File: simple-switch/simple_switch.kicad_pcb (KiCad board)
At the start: 4 copper layers, 25.4 x 40.6 mm, 20 parts, among them J1 CON_HDR_100MILS_M_TH_2X8, J2 CON_TERM_BLK_1X2_TB008A-508-0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, Q1 TRX_NMOS_PJD40N04_L2_00001, Q2 TRX_NMOS_PJD40N04_L2_00001, Q3 TRX_NMOS_PJD40N04_L2_00001, Q4 TRX_NMOS_PJD40N04_L2_00001, U1 DRV_A4957SESTR-T

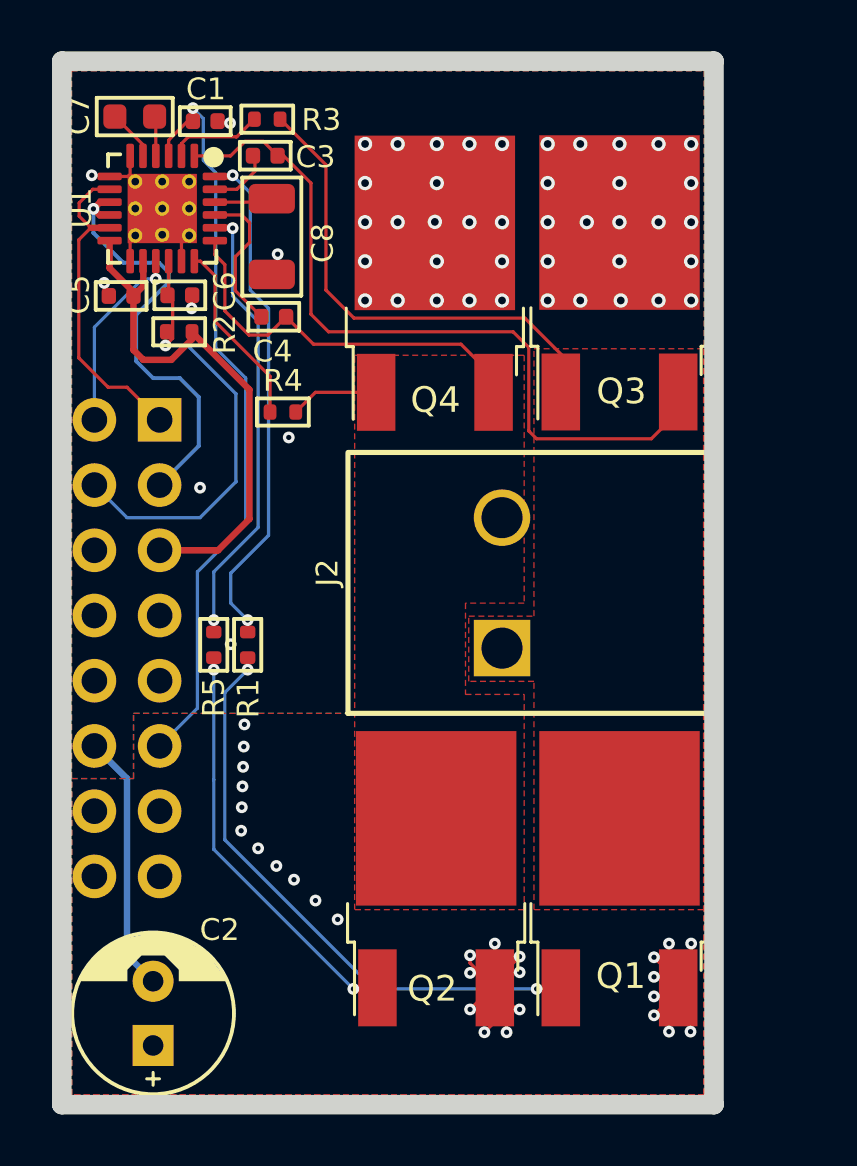
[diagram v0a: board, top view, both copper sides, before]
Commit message: rename project, comple simple switch layout, fix thermal reliefs
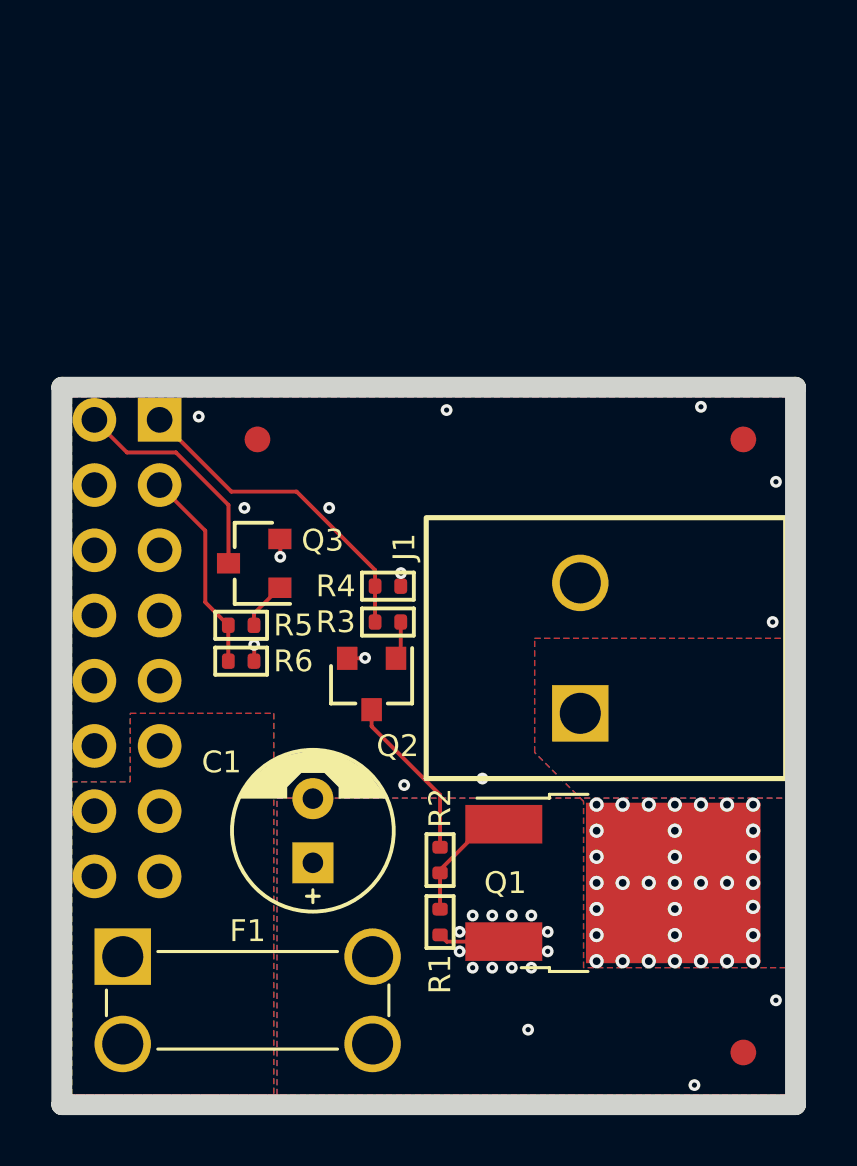
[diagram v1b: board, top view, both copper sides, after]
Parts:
- removed C2: CAP_AE_22UF_100V_TH_6.3MM, connaxio-capacitors:CAP_AE_RAD_D6.3_H12.5_P2.5
- removed C3, C4, C5, C6: CAP_CER_100NF_25V_0402, connaxio-capacitors:CAP_CER_0402_1005M
- removed C7: CAP_CER_1UF_25V_0603, connaxio-capacitors:CAP_CER_0603_1608M
- removed C8: CAP_CER_10UF_25V_1206, connaxio-capacitors:CAP_CER_1206_3216M
- removed Q4: TRX_NMOS_PJD40N04_L2_00001, connaxio-sop:TO-252-3
- removed U1: DRV_A4957SESTR-T, connaxio-fp:QFN-24_4x4_P0.5_EP2.7X2.7
- added F1: FUS_BLADE_MINI_3588-1, connaxio-connectors:FUS_BLADE_MINI_3588-1, F.Cu at (121.2, 84.8)
- added F2: FID_1X3, connaxio-mechanical:FID_1X3, F.Cu at (121.5, 63.0)
- added F3: FID_1X3, connaxio-mechanical:FID_1X3, F.Cu at (140.5, 63.0)
- added F4: FID_1X3, connaxio-mechanical:FID_1X3, F.Cu at (140.5, 86.9)
- added R6: RES_12.4KΩ_1%_0402, connaxio-resistors:RES_0402_1005M, F.Cu at (120.9, 71.6)
- C1: value CAP_CER_100NF_25V_0402 -> CAP_AE_22UF_100V_TH_6.3MM; footprint connaxio-capacitors:CAP_CER_0402_1005M -> connaxio-capacitors:CAP_AE_RAD_D6.3_H12.5_P2.5
- J1: value CON_HDR_100MILS_M_TH_2X8 -> CON_TERM_BLK_1X2_TB008A-508-02BE; footprint connaxio-connectors:CON_HDR_100MILS_M_TH_2X8 -> connaxio-connectors:CON_TERM_BLK_1X2_TB008A-508-02BE; moved to F.Cu
- J2: value CON_TERM_BLK_1X2_TB008A-508-02BE -> CON_HDR_100MILS_M_TH_2X8; footprint connaxio-connectors:CON_TERM_BLK_1X2_TB008A-508-02BE -> connaxio-connectors:CON_HDR_100MILS_M_TH_2X8; moved to B.Cu
- Q1: value TRX_NMOS_PJD40N04_L2_00001 -> TRX_PMOS_AOD4189
- Q2, Q3: value TRX_NMOS_PJD40N04_L2_00001 -> TRX_NPN_MMBT3904-TP; footprint connaxio-sop:TO-252-3 -> connaxio-sop:SOT-23-3
- R1, R4: value RES_226Ω_1%_0402 -> RES_12.4KΩ_1%_0402
- R2: value RES_5.10KΩ_1%_0402 -> RES_12.4KΩ_1%_0402
- R3, R5: value RES_226Ω_1%_0402 -> RES_1.54KΩ_1%_0402
- moved C1 28.0 mm to (123.7, 78.2), turned to 90 degrees
- moved R2 22.9 mm to (128.7, 79.4), turned to 90 degrees
- moved R3 20.1 mm to (126.6, 70.1), turned to 0 degrees
- moved Q3 17.9 mm to (121.4, 67.8), turned to 180 degrees
- moved J1 17.7 mm to (134.1, 71.1), turned to 90 degrees
- moved J2 14.8 mm to (116.5, 71.1), turned to 180 degrees
- moved R1 13.1 mm to (128.7, 81.8), turned to 90 degrees
- moved Q2 7.99 mm to (126.0, 72.5), turned to -90 degrees
- moved R4 7.92 mm to (126.6, 68.7)
- moved R5 1.31 mm to (120.9, 70.2), turned to 0 degrees
- moved Q1 0.31 mm to (135.4, 80.3), turned to -90 degrees
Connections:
- J1 pad 1: /CTRLA -> Net-(J1-Pad1)
- J1 pad 2: /FAULT -> GND
- J2 pad 1: /OUTA -> /CTRLA
- J2 pad 2: /OUTB -> /FAULT
- Q1 pad 3: /OUTA -> Net-(J1-Pad1)
- Q2 pad 2: Vdrive -> GND
- Q2 pad 3: /OUTB -> Net-(Q2-Pad3)
- Q3 pad 2: /OUTA -> GND
- Q3 pad 3: GND -> /FAULT
- R1 pad 1: Net-(R1-Pad1) -> Vdrive
- R2 pad 1: +3.3V -> Net-(Q1-Pad1)
- R2 pad 2: /RST -> Net-(Q2-Pad3)
- R3 pad 1: Net-(Q3-Pad1) -> /CTRLA
- R3 pad 2: Net-(R3-Pad2) -> Net-(Q2-Pad1)
- R4 pad 1: Net-(R4-Pad1) -> /CTRLA
- R4 pad 2: Net-(Q4-Pad1) -> GND
- R5 pad 1: Net-(R5-Pad1) -> /CTRLB
- R5 pad 2: Net-(Q2-Pad1) -> Net-(Q3-Pad1)
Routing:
- net Vdrive: track 56.0 -> 2.59 mm, vias 29 -> 15
- net /OUTA: track 30.0 -> 0.00 mm
- net +3.3V: track 21.4 -> 0.00 mm
- net Net-(R1-Pad1): track 20.0 -> 0.00 mm, vias 2 -> 0
- net GND: track 21.0 -> 2.55 mm, vias 49 -> 13
- net Net-(Q1-Pad1): track 23.0 -> 4.75 mm, vias 2 -> 0
- net Net-(R5-Pad1): track 17.5 -> 0.00 mm, vias 2 -> 0
- net Net-(Q3-Pad1): track 19.1 -> 1.88 mm
- net /RST: track 17.1 -> 0.00 mm, vias 1 -> 0
- net /OUTB: track 15.6 -> 0.00 mm
- net Net-(Q2-Pad1): track 16.2 -> 1.49 mm, vias 2 -> 0
- net /CTRLB: track 17.0 -> 7.97 mm, vias 1 -> 0
- net Net-(R4-Pad1): track 7.24 -> 0.00 mm
- net Net-(Q2-Pad3): track 0.00 -> 6.46 mm
- net Net-(C4-Pad1): track 5.79 -> 0.00 mm
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- added copper zone on B.Cu, net Net-(F1-Pad1)
- added copper zone on F.Cu, net Net-(F1-Pad1)
- added copper zone on In1.Cu, net Net-(F1-Pad1)
- added copper zone on In2.Cu, net Net-(F1-Pad1)
- added copper zone on B.Cu, net Net-(J1-Pad1)
- added copper zone on F.Cu, net Net-(J1-Pad1)
- added copper zone on In1.Cu, net Net-(J1-Pad1)
- added copper zone on In2.Cu, net Net-(J1-Pad1)
- removed copper zone on F.Cu, net /OUTA
- removed copper zone on F.Cu, net /OUTB
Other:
- board size 25.4 x 40.6 mm -> 28.6 x 27.9 mm

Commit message: Inverted motor controls for open-drain operation and manual switch override compatibility
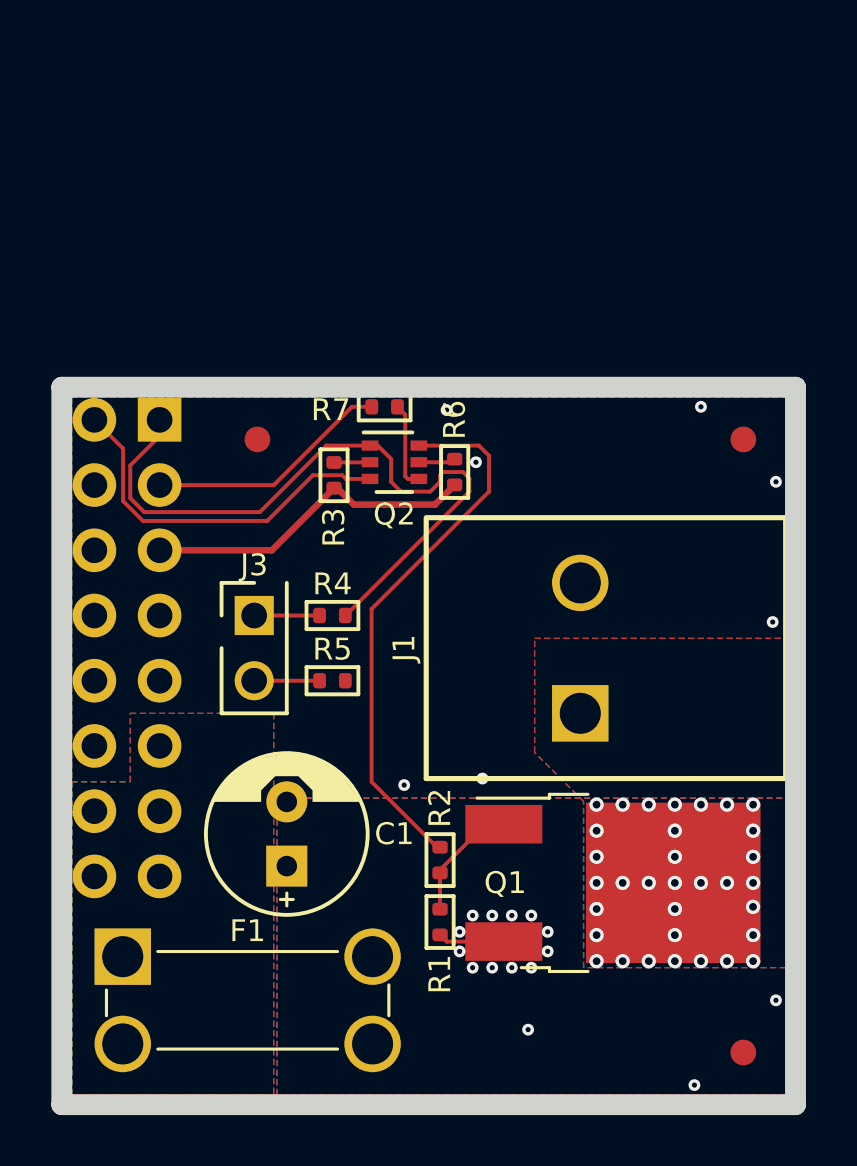
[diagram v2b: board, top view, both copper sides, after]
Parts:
- removed Q3: TRX_NPN_MMBT3904-TP, connaxio-sop:SOT-23-3
- added J3: CON_HDR_100MILS_M_TH_1X2, connaxio-connectors:CON_HDR_100MILS_M_TH_1X2, F.Cu at (121.4, 71.1)
- added R7: RES_226Ω_1%_0402, connaxio-resistors:RES_0402_1005M, F.Cu at (126.5, 61.7)
- Q2: value TRX_NPN_MMBT3904-TP -> TRX_2NPN_BC846S,115; footprint connaxio-sop:SOT-23-3 -> connaxio-sop:SOT-363_SC-70-6
- R3: value RES_1.54KΩ_1%_0402 -> RES_12.4KΩ_1%_0402
- R4: value RES_12.4KΩ_1%_0402 -> RES_226Ω_1%_0402
- R5: value RES_1.54KΩ_1%_0402 -> RES_226Ω_1%_0402
- moved R6 11.1 mm to (129.2, 64.3), turned to 90 degrees
- moved Q2 8.68 mm to (126.9, 63.9), turned to 0 degrees
- moved R3 6.09 mm to (124.5, 64.4), turned to 90 degrees
- moved R5 4.16 mm to (124.5, 72.4)
- moved R4 2.44 mm to (124.5, 69.8)
- moved C1 1.02 mm to (122.7, 78.4)
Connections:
- J2 pad 1: /CTRLA -> /~{CTRLA}
- J2 pad 2: /FAULT -> /~{FAULT}
- J2 pad 3: /CTRLB -> /~{CTRLB}
- J2 pad 4: /RST -> unconnected-(J2-Pad4)
- Q2 pad 1: Net-(Q2-Pad1) -> /~{CTRLA}
- Q2 pad 2: GND -> Net-(Q2-Pad2)
- Q2 pad 3: Net-(Q2-Pad3) -> /~{FAULT}
- R2 pad 2: Net-(Q2-Pad3) -> /PMOS_CTRL
- R3 pad 1: /CTRLA -> +3.3V
- R3 pad 2: Net-(Q2-Pad1) -> Net-(Q2-Pad2)
- R4 pad 1: /CTRLA -> Net-(J3-Pad1)
- R4 pad 2: GND -> /~{CTRLA}
- R5 pad 1: /CTRLB -> Net-(J3-Pad2)
- R5 pad 2: Net-(Q3-Pad1) -> GND
- R6 pad 1: /CTRLB -> +3.3V
- R6 pad 2: GND -> Net-(Q2-Pad5)
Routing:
- net /~{CTRLA}: track 0.00 -> 27.2 mm
- net /PMOS_CTRL: track 0.00 -> 21.2 mm
- net /~{FAULT}: track 0.00 -> 14.4 mm
- net +3.3V: track 0.00 -> 13.1 mm
- net /CTRLA: track 12.8 -> 0.00 mm
- net /~{CTRLB}: track 0.00 -> 9.53 mm
- net /FAULT: track 8.87 -> 0.00 mm
- net /CTRLB: track 7.97 -> 0.00 mm
- net Net-(Q2-Pad3): track 6.46 -> 0.00 mm
- net Net-(Q2-Pad4): track 0.00 -> 3.40 mm
- net GND: track 2.55 -> 0.00 mm, vias 13 -> 7
- net Net-(J3-Pad2): track 0.00 -> 2.55 mm
- net Net-(J3-Pad1): track 0.00 -> 2.55 mm
- net Net-(Q3-Pad1): track 1.88 -> 0.00 mm
- net Net-(Q2-Pad1): track 1.49 -> 0.00 mm
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
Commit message: Add LEDs, fix NMOS, Add logos and infos on PCBs.
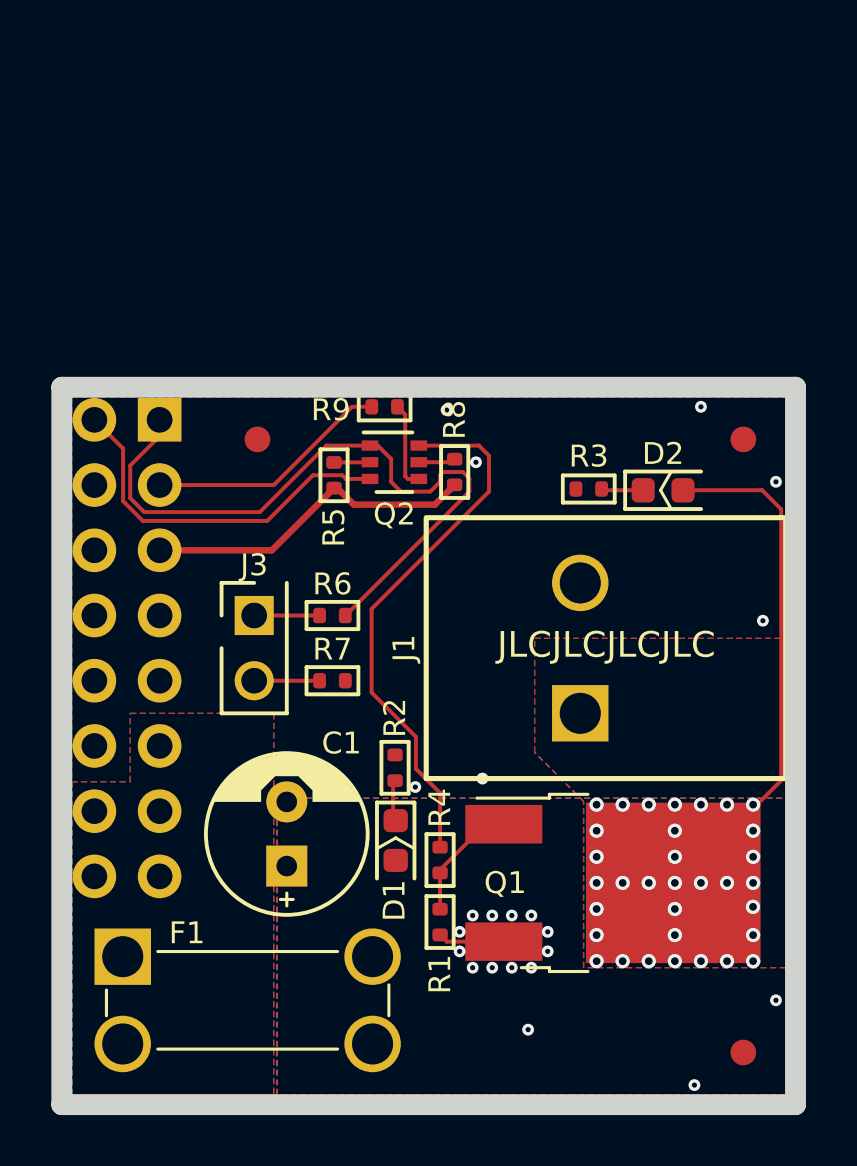
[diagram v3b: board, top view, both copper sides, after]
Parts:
- added D1: DIO_LED_GREEN_150060GS75000, connaxio-diodes:LED_0603_1608M, F.Cu at (126.9, 78.6)
- added D2: DIO_LED_GREEN_150060GS75000, connaxio-diodes:LED_0603_1608M, F.Cu at (137.3, 65.0)
- added G***: LOGO, LOGO, B.Cu at (132.0, 63.4)
- added G***: LOGO, LOGO, B.Cu at (138.6, 68.3)
- added R2: RES_5.10KΩ_1%_0402, connaxio-resistors:RES_0402_1005M, F.Cu at (126.9, 75.8)
- added R3: RES_5.10KΩ_1%_0402, connaxio-resistors:RES_0402_1005M, F.Cu at (134.4, 64.9)
- renumbered R2 to R4, R3 to R5, R4 to R6, R5 to R7, R6 to R8, R7 to R9
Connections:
- net Net-(J1-Pad1) renamed /VOUT
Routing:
- net /VOUT: track 0.00 -> 20.5 mm
- net Net-(D2-Pad1): track 0.00 -> 1.64 mm
- net Net-(D1-Pad1): track 0.00 -> 1.60 mm
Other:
- board text added: "${title} Rev ${rev} ${year}-${month} Licensed under CERN-OHL-W v2"
- board text added: "JLCJLCJLCJLC"
- board text added: "https://github.com/ Connaxio/production- controller-makroshield"

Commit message: Add Enclosure piercing guide and fix h-bridge-driver NMOS pads.
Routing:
- removed copper zone on In1.Cu, net /VOUT
- removed copper zone on In2.Cu, net /VOUT
- removed copper zone on In1.Cu, net GND
- removed copper zone on In2.Cu, net GND
- removed copper zone on In1.Cu, net Net-(F1-Pad1)
- removed copper zone on In2.Cu, net Net-(F1-Pad1)
- removed copper zone on In1.Cu, net Vdrive
- removed copper zone on In2.Cu, net Vdrive
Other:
- copper layers 4 -> 2
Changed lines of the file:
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@@
 (kicad_pcb (version 20211014) (generator pcbnew)
   (general
-    (thickness 1.6062)
+    (thickness 0.3004)
   )
   (paper "A4")
@@
   (layers
     (0 "F.Cu" signal)
-    (1 "In1.Cu" power)
-    (2 "In2.Cu" power)
     (31 "B.Cu" signal)
     (35 "F.Paste" user)
@@
       (layer "F.Cu" (type "copper") (thickness 0.035))
       (layer "dielectric 1" (type "core") (thickness 0.2104) (material "FR4") (epsilon_r 4.6) (loss_tangent 0.02))
-      (layer "In1.Cu" (type "copper") (thickness 0.0152))
-      (layer "dielectric 2" (type "prepreg") (thickness 1.065) (material "FR4") (epsilon_r 4.6) (loss_tangent 0.02))
-      (layer "In2.Cu" (type "copper") (thickness 0.0152))
-      (layer "dielectric 3" (type "core") (thickness 0.2104) (material "FR4") (epsilon_r 4.6) (loss_tangent 0.02))
       (layer "B.Cu" (type "copper") (thickness 0.035))
       (layer "B.Mask" (type "Bottom Solder Mask") (color "Green") (thickness 0.01))
@@
   (via (at 139.827 80.264) (size 0.56) (drill 0.3) (layers "F.Cu" "B.Cu") (net 19))
   (via (at 135.763 83.312) (size 0.56) (drill 0.3) (layers "F.Cu" "B.Cu") (net 19))
-  (zone (net 6) (net_name "Vdrive") (layers "F.Cu" "In1.Cu" "In2.Cu" "B.Cu") (hatch edge 0.508)
+  (zone (net 6) (net_name "Vdrive") (layers F&B.Cu) (hatch edge 0.508)
     (priority 2)
     (connect_pads (clearance 0.127))
@@
     )
   )
-  (zone (net 2) (net_name "GND") (layers "F.Cu" "In1.Cu" "In2.Cu" "B.Cu") (hatch edge 0.508)
+  (zone (net 2) (net_name "GND") (layers F&B.Cu) (hatch edge 0.508)
     (connect_pads (clearance 0.127))
     (min_thickness 0.127) (filled_areas_thickness no)
@@
     )
   )
-  (zone (net 19) (net_name "/VOUT") (layers "F.Cu" "In1.Cu" "In2.Cu" "B.Cu") (hatch edge 0.508)
+  (zone (net 19) (net_name "/VOUT") (layers F&B.Cu) (hatch edge 0.508)
     (priority 3)
     (connect_pads (clearance 0.127))
@@
     )
   )
-  (zone (net 3) (net_name "Net-(F1-Pad1)") (layers "F.Cu" "In1.Cu" "In2.Cu" "B.Cu") (hatch edge 0.508)
+  (zone (net 3) (net_name "Net-(F1-Pad1)") (layers F&B.Cu) (hatch edge 0.508)
     (priority 1)
     (connect_pads (clearance 0.127))
